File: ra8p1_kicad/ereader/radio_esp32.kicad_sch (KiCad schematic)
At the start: 11 parts, among them U3 ESP32-C6-WROOM-1-N8, U4 TPS22917DBVT, U5 TXU0304PWR

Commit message: Define radio SPI idle bias with linked engineering calculations
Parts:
- added R10, R9: 10k, symbol Device:R
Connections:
- net +3V3_RADIO: now also R10.1
- net C6_CS_N: now also R10.2
- net GND: now also R9.2
- net at U5.8 (OE): now also R9.1
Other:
- note added: "RADIO-010: R9/R10 idle-state bias, 10k 1% Rmin/max = 10k*(1 +/-1%)*(1 +/-1%) = 9801/10201 ohm. 12 uA adverse leakage is an ALLOCATION, not measured. R9: Vlow = 12u*10201 = 0.122412 V. TI VT- min = 0.17 V at the 1.1 V equal-rail test point. R10 @3.3 V: VCS >=3.177588 V > VIH 2.475 V (25 C). R9 enabled current = 3.3/10k = 0.330 mA. R10 draws similar current only while CS is low. OE arbitration, all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"

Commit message: Add radio supervisor candidate and linked threshold calculations
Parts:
- added C51: 100n, symbol Device:C_Small
- added U6: TPS389001DSET, symbol Power_Devices:TPS389001DSET
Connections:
- net +3V3_MCU: now also C51.1, U6.4 (VDD)
- net GND: now also C51.2, U6.2 (GND)
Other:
- note added: "RADIO-011: U6 supervisor threshold screen C51: 100 nF VDD bypass per TI TPS3890 section 6. Example divider 33.2k / 20k is NOT FITTED or approved. Assume 0.1%, 25 ppm/C, deltaT=100 C, +/-100 nA. fmin=0.9965025; fmax=1.0035025. Vtrip = Vsense*(1 + Rt/Rb) + Is*Rt. Worst falling screen = 3.011895176 V. Worst rising screen = 3.132066484 V. Loaded-rail screen 3.1465 V leaves only 14.434 mV. Divider, CT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"

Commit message: Derive main-rail feedback and reset headroom budget
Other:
- note added: "PWR-002: upstream regulator / reset voltage budget TPS63802 candidate: +/-1% feedback applies in PWM mode. Example 56k/10k, 0.1%, 25 ppm/C; deltaT=100 C. Vout = Vfb*(1+Rt/Rb) + Ib*Rt; allocate +/-100 nA. PWM static screen: 3.242044..3.358485 V. Radio: 3.242044 - 0.5 A*0.175 ohm = 3.154544 V. Above U6 rising screen: only 22.478 mV remains. MCU reset release headroom: 48.093 mV. Not a transient gua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"
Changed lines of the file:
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@@
 		(comment 1 "Incomplete electrical design - not for manufacture")
+	)
+	(text "PWR-002: upstream regulator / reset voltage budget\nTPS63802 candidate: +/-1% feedback applies in PWM mode.\nExample 56k/10k, 0.1%, 25 ppm/C; deltaT=100 C.\nVout = Vfb*(1+Rt/Rb) + Ib*Rt; allocate +/-100 nA.\nPWM static screen: 3.242044..3.358485 V.\nRadio: 3.242044 - 0.5 A*0.175 ohm = 3.154544 V.\nAbove U6 rising screen: only 22.478 mV remains.\nMCU reset release headroom: 48.093 mV.\nNot a transient guarantee; regulator circuit not fitted.\nMath: ../design/power_decoupling.md#pwr-002-main-rail-regulation-and-reset-headroom"
+		(exclude_from_sim no)
+		(at 266.7 142.24 0)
+		(effects
+			(font
+				(size 1.27 1.27)
+			)
+			(justify left top)
+			(href "https://github.com/bsikar/ra8-firmware/blob/design/ereader-circuit/ra8p1_kicad/design/power_decoupling.md#pwr-002-main-rail-regulation-and-reset-headroom")
+		)
 	)
 	(text "RADIO-009: U5 isolates host and switched-radio signal domains.\nC49/C50: 100 nF local bypass; TI TXU0304 section 12.1.\nC50 adds 0.1 uF: fitted external radio capacitance = 10.2 uF nominal.\n5 MHz budget: 100 - 11 - 11 = 78 ns remaining (5 pF test load).\nSPI/OE and reset qualification remain open; timing is not closed.\nMath: ../design/radio_interface.md#radio-009-spi-power-domain-isolation"

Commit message: Implement radio supervisor delay capacitor with verified calculations
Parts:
- added C52: 1n, symbol Device:C_Small
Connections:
- net GND: now also C52.1
- net at U6.5 (CT): now also C52.2
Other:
- note added: "RADIO-011: U6 supervisor threshold screen C51: 100 nF VDD bypass per TI TPS3890 section 6. Example divider 33.2k / 20k is NOT FITTED or approved. Assume 0.1%, 25 ppm/C, deltaT=100 C, +/-100 nA. fmin=0.9965025; fmax=1.0035025. Vtrip = Vsense*(1 + Rt/Rb) + Is*Rt. Worst falling screen = 3.011895176 V. Worst rising screen = 3.132066484 V. Loaded-rail screen 3.1465 V leaves only 14.434 mV. C52 delay: 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"
- note added: "RADIO-012: C52 / U6 reset-release delay C52 = 1nF +/-5% NP0, CT to GND (not VIN). At 100 C excursion, +/-30 ppm/C: 947.15..1053.15 pF. tnom = 1nF*1.23V/1.15uA + 25us = 1.094565 ms. Allocate +/-10nA external CT leakage; start discharged. tcharge_min = 947.15pF*1.17V/1.36uA = 814.828 us. tcharge_max = 1053.15pF*1.29V/0.89uA = 1526.476 us. Charge-only screen, NOT total reset min/max limits. C6 requi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"
- note removed: "RADIO-011: U6 supervisor threshold screen C51: 100 nF VDD bypass per TI TPS3890 section 6. Example divider 33.2k / 20k is NOT FITTED or approved. Assume 0.1%, 25 ppm/C, deltaT=100 C, +/-100 nA. fmin=0.9965025; fmax=1.0035025. Vtrip = Vsense*(1 + Rt/Rb) + Is*Rt. Worst falling screen = 3.011895176 V. Worst rising screen = 3.132066484 V. Loaded-rail screen 3.1465 V leaves only 14.434 mV. Divider, CT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"

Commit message: Connect radio reset output with verified enable pull-up
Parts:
- added R11: 10k, symbol Device:R
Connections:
- net +3V3_RADIO: now also R11.1
- net C6_EN: now reaches U6.6 (~{RESET})
- net C6_EN: now also U3.3 (EN), R11.2
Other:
- note added: "RADIO-013: R11 / C6_EN reset pull-up 10k 1%, 100ppm/C; deltaT=100 C allocation. Rmin/max=10k*(1 +/-1%)*(1 +/-1%)=9801/10201 ohm. Allocate +/-12uA total adverse node leakage. Isink <=3.6/9801+12uA=0.379310mA <0.4mA. U6 VOL<=0.25V at 0.4mA, VDD>=1.5V. At C6 table point 3.3V, 25 C: VEN>=3.3-12uA*10201=3.177588V >2.475V VIH. VIL=0.825V; low margin=0.825-0.25=0.575V. Pmax=3.6^2/9801=1.322314mW. MR/SEN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"

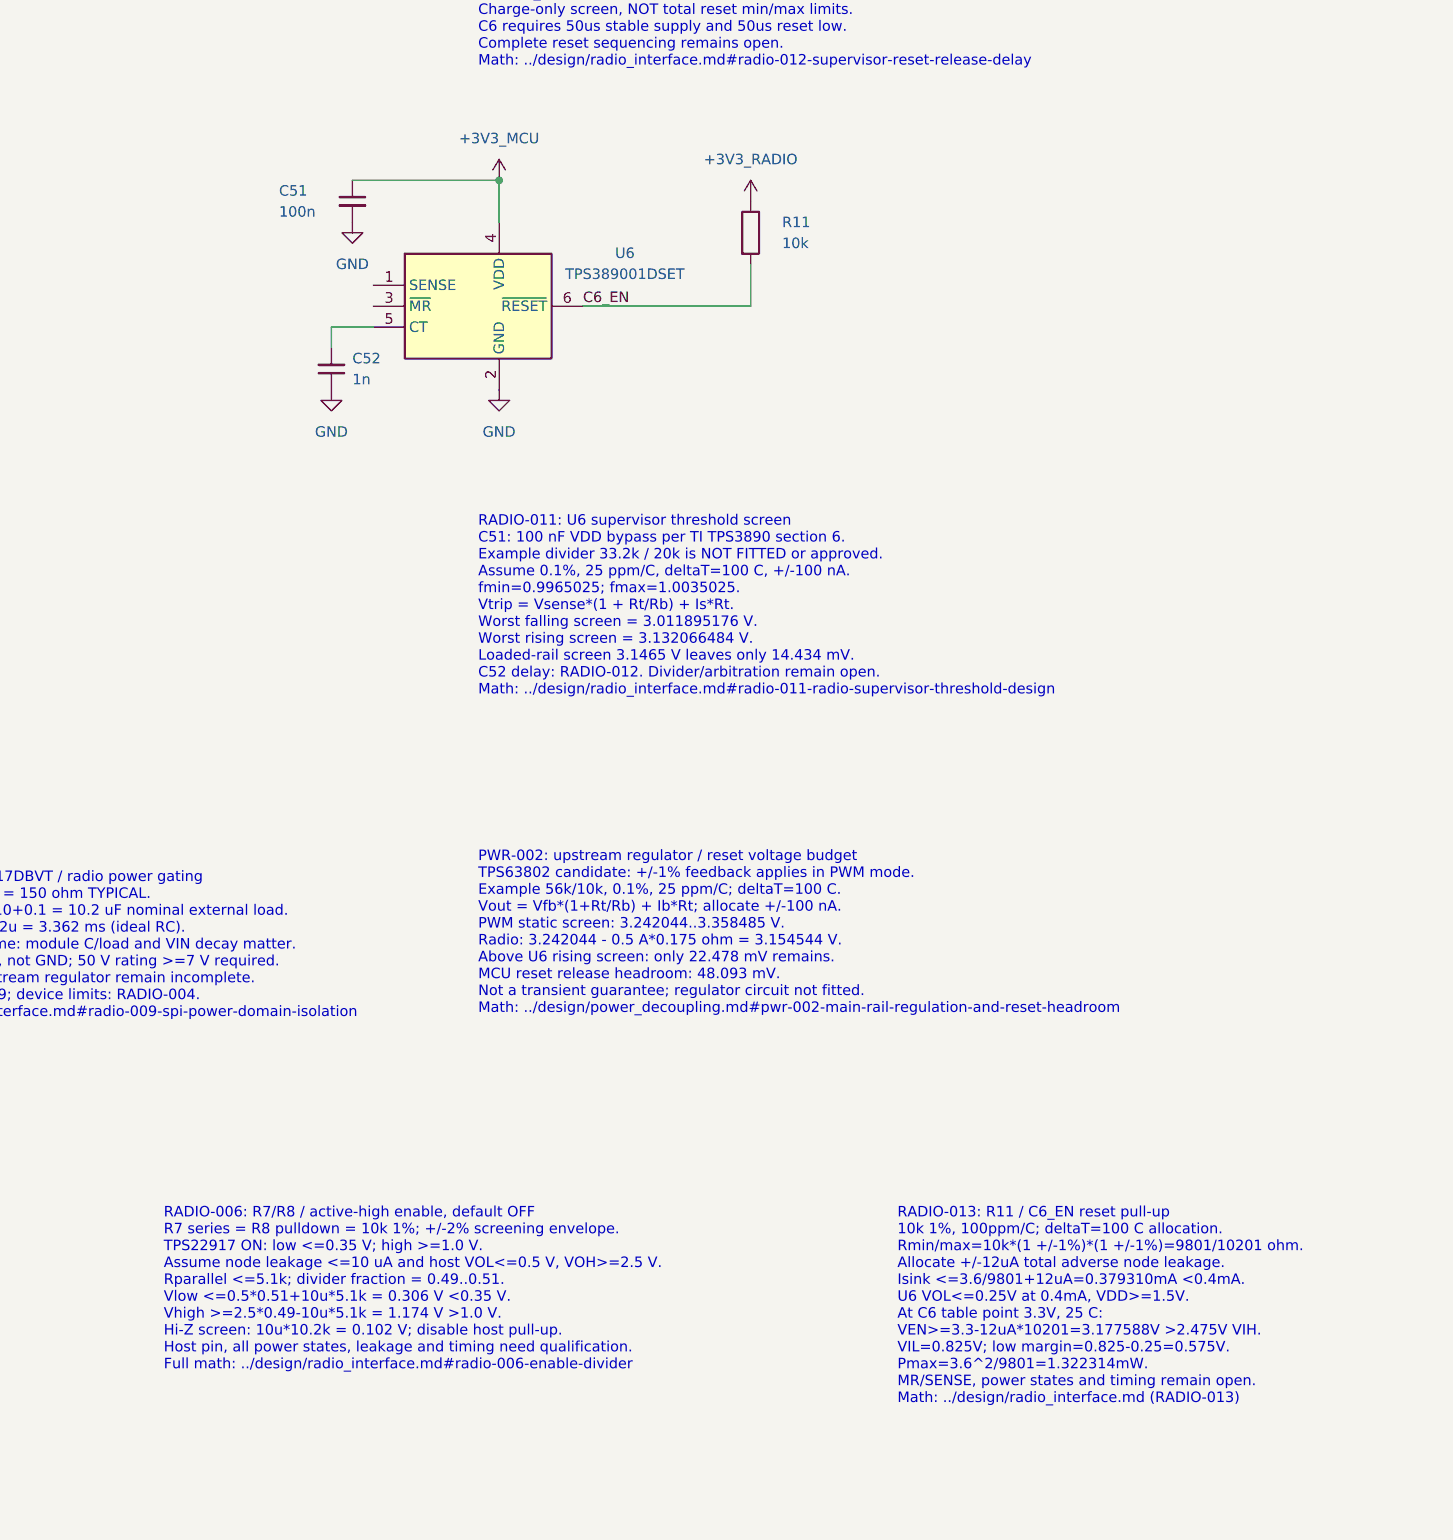
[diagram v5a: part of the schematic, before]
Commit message: Implement radio sense divider with extended tolerance budget
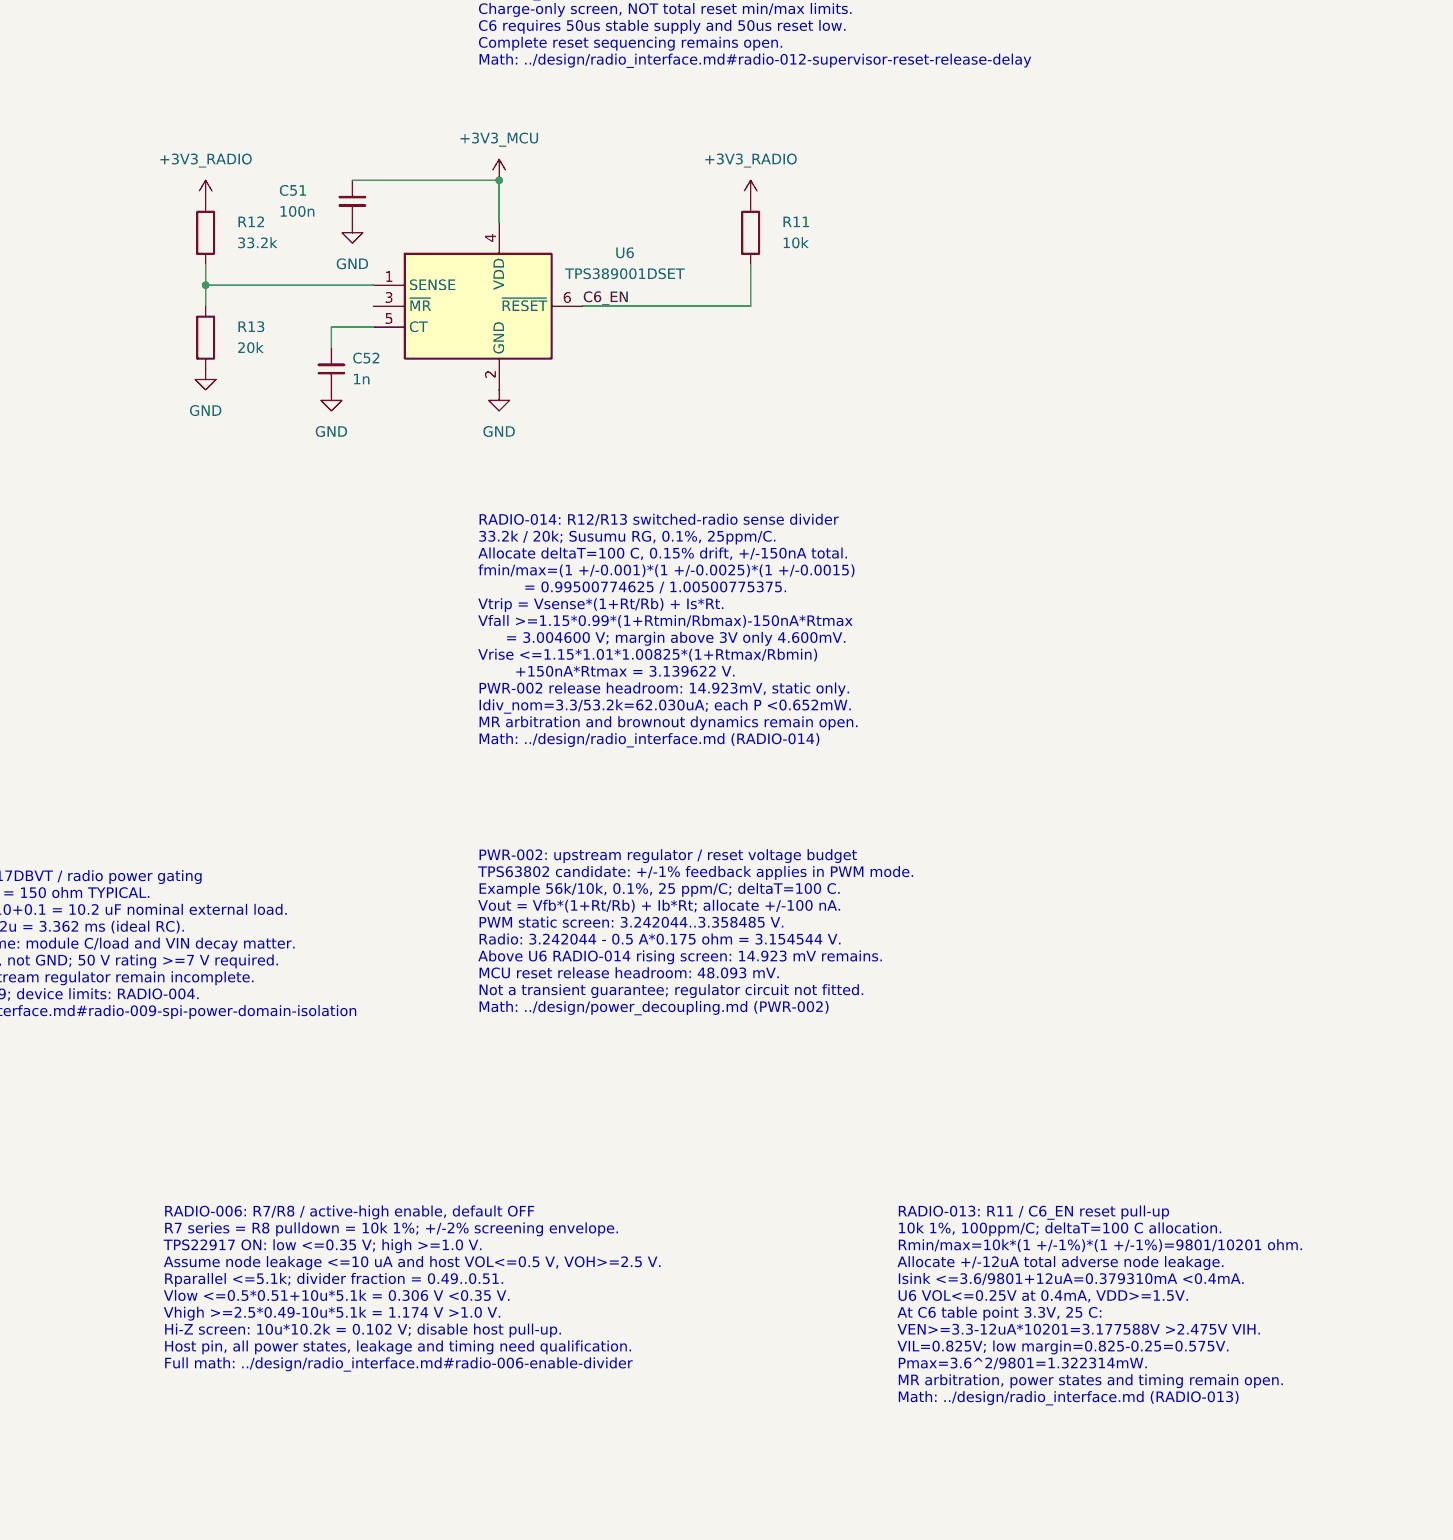
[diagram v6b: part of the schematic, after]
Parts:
- added R12: 33.2k, symbol Device:R
- added R13: 20k, symbol Device:R
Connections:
- net +3V3_RADIO: now also R12.1
- net GND: now also R13.2
- net at U6.1 (SENSE): now also R12.2, R13.1
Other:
- note added: "PWR-002: upstream regulator / reset voltage budget TPS63802 candidate: +/-1% feedback applies in PWM mode. Example 56k/10k, 0.1%, 25 ppm/C; deltaT=100 C. Vout = Vfb*(1+Rt/Rb) + Ib*Rt; allocate +/-100 nA. PWM static screen: 3.242044..3.358485 V. Radio: 3.242044 - 0.5 A*0.175 ohm = 3.154544 V. Above U6 RADIO-014 rising screen: 14.923 mV remains. MCU reset release headroom: 48.093 mV. Not a transien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"
- note added: "RADIO-013: R11 / C6_EN reset pull-up 10k 1%, 100ppm/C; deltaT=100 C allocation. Rmin/max=10k*(1 +/-1%)*(1 +/-1%)=9801/10201 ohm. Allocate +/-12uA total adverse node leakage. Isink <=3.6/9801+12uA=0.379310mA <0.4mA. U6 VOL<=0.25V at 0.4mA, VDD>=1.5V. At C6 table point 3.3V, 25 C: VEN>=3.3-12uA*10201=3.177588V >2.475V VIH. VIL=0.825V; low margin=0.825-0.25=0.575V. Pmax=3.6^2/9801=1.322314mW. MR arb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"
- note added: "RADIO-014: R12/R13 switched-radio sense divider 33.2k / 20k; Susumu RG, 0.1%, 25ppm/C. Allocate deltaT=100 C, 0.15% drift, +/-150nA total. fmin/max=(1 +/-0.001)*(1 +/-0.0025)*(1 +/-0.0015) = 0.99500774625 / 1.00500775375. Vtrip = Vsense*(1+Rt/Rb) + Is*Rt. Vfall >=1.15*0.99*(1+Rtmin/Rbmax)-150nA*Rtmax = 3.004600 V; margin above 3V only 4.600mV. Vrise <=1.15*1.01*1.00825*(1+Rtmax/Rbmin) +150nA*Rtma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"
- note removed: "PWR-002: upstream regulator / reset voltage budget TPS63802 candidate: +/-1% feedback applies in PWM mode. Example 56k/10k, 0.1%, 25 ppm/C; deltaT=100 C. Vout = Vfb*(1+Rt/Rb) + Ib*Rt; allocate +/-100 nA. PWM static screen: 3.242044..3.358485 V. Radio: 3.242044 - 0.5 A*0.175 ohm = 3.154544 V. Above U6 rising screen: only 22.478 mV remains. MCU reset release headroom: 48.093 mV. Not a transient gua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"
- note removed: "RADIO-011: U6 supervisor threshold screen C51: 100 nF VDD bypass per TI TPS3890 section 6. Example divider 33.2k / 20k is NOT FITTED or approved. Assume 0.1%, 25 ppm/C, deltaT=100 C, +/-100 nA. fmin=0.9965025; fmax=1.0035025. Vtrip = Vsense*(1 + Rt/Rb) + Is*Rt. Worst falling screen = 3.011895176 V. Worst rising screen = 3.132066484 V. Loaded-rail screen 3.1465 V leaves only 14.434 mV. C52 delay: 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"
- note removed: "RADIO-013: R11 / C6_EN reset pull-up 10k 1%, 100ppm/C; deltaT=100 C allocation. Rmin/max=10k*(1 +/-1%)*(1 +/-1%)=9801/10201 ohm. Allocate +/-12uA total adverse node leakage. Isink <=3.6/9801+12uA=0.379310mA <0.4mA. U6 VOL<=0.25V at 0.4mA, VDD>=1.5V. At C6 table point 3.3V, 25 C: VEN>=3.3-12uA*10201=3.177588V >2.475V VIH. VIL=0.825V; low margin=0.825-0.25=0.575V. Pmax=3.6^2/9801=1.322314mW. MR/SEN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"
